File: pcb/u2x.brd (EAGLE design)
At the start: 100 x 100 mm, 9 parts, among them IC4 REG1117, SW20 324_SW, U1 UG-2864HSWEG01, U2 CY8C5868LTI-LP039, U3 USBC_16P

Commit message: started working on pcb
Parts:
- removed U1: UG-2864HSWEG01, lul:LUL_UG-2864HSWEG01_1.3_WRAPAROUND
- removed X2: (no value), bott:USB-A-H
- added JP1: (no value), adafruit_changed:2X20-BIG
- added X8: USB2, RPB:USB2
- X1: value (none) -> USB2; device bott:USB-A-H -> RPB:USB2
- moved X1 85.3 mm to (27.2, 3.05), turned to 90 degrees
- moved X3 62.3 mm to (8.89, 3.05), turned to 90 degrees
- moved SW20 23.6 mm to (5.08, 55.1)
- moved IC4 20.7 mm to (5.59, 63.8), turned to 90 degrees
- moved U2 14.0 mm to (31.0, 49.3)
- moved SD1 3.89 mm to (8.03, 18.9)
- moved U3 0.25 mm to (5.46, 47.0)
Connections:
- removed net VCC: U1.28
- removed net VLSS: U1.29
- net VDD: no longer U1.9
- net VSS: no longer U1.31, U1.32, U1.8
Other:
- board size 100 x 100 mm -> 56 x 85 mm
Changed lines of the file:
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@@
 <board>
 <plain>
-<wire x1="0" y1="100" x2="0" y2="0" width="0" layer="20"/>
-<wire x1="0" y1="0" x2="100" y2="0" width="0" layer="20"/>
-<wire x1="100" y1="0" x2="100" y2="100" width="0" layer="20"/>
-<wire x1="100" y1="100" x2="0" y2="100" width="0" layer="20"/>
-<rectangle x1="22.4834" y1="56.8782" x2="56.4834" y2="79.8782" layer="51"/>
-<rectangle x1="19.372" y1="28.992" x2="59.372" y2="43.992" layer="51" rot="R90"/>
-<rectangle x1="62.23" y1="40.894" x2="81.83" y2="65.894" layer="51"/>
+<wire x1="0" y1="85" x2="0" y2="0" width="0" layer="20"/>
+<wire x1="0" y1="0" x2="56" y2="0" width="0" layer="20"/>
+<wire x1="56" y1="0" x2="56" y2="85" width="0" layer="20"/>
+<wire x1="56" y1="85" x2="0" y2="85" width="0" layer="20"/>
 </plain>
 <attributes>
@@
 </autorouter>
 <elements>
-<element name="U3" library="my_usbc_16p" package="USBC_16P_FOOT" value="USBC_16P" x="5.461" y="47.2186" smashed="yes" rot="R270"/>
-<element name="U1" library="lul" package="LUL_UG-2864HSWEG01_1.3_WRAPAROUND" value="UG-2864HSWEG01" x="41.0784" y="7.5306" smashed="yes" rot="MR180"/>
-<element name="SD1" library="clock" package="TF-PULL" value="TF-HOLDER" x="8.7884" y="22.7076" smashed="yes" rot="R90">
-<attribute name="NAME" x="7.6884" y="30.4076" size="1.016" layer="25" ratio="18"/>
-</element>
-<element name="IC4" library="clock" package="SOT223" value="REG1117" x="19.05" y="48.006" smashed="yes" rot="R270">
-<attribute name="MF" value="" x="31.75" y="55.626" size="1.778" layer="27" rot="R270" display="off"/>
-<attribute name="MPN" value="REG1117" x="31.75" y="55.626" size="1.778" layer="27" rot="R270" display="off"/>
-<attribute name="NAME" x="23.368" y="50.546" size="1.27" layer="25" ratio="10" rot="R270"/>
-<attribute name="OC_FARNELL" value="1097566" x="31.75" y="55.626" size="1.778" layer="27" rot="R270" display="off"/>
-<attribute name="OC_NEWARK" value="14P6981" x="31.75" y="55.626" size="1.778" layer="27" rot="R270" display="off"/>
-<attribute name="VALUE" x="13.208" y="50.8" size="1.27" layer="27" ratio="10" rot="R270"/>
-</element>
-<element name="SW20" library="3pos_slide_switch_centered" package="342_SWICH_FOOT" value="324_SW" x="20.066" y="36.83" smashed="yes"/>
-<element name="X1" library="bott" package="USB-A-H" value="" x="36.322" y="87.884" smashed="yes" rot="R270">
-<attribute name="NAME" x="40.132" y="82.169" size="1.27" layer="25"/>
-</element>
-<element name="X2" library="bott" package="USB-A-H" value="" x="12.192" y="84.582" smashed="yes">
-<attribute name="NAME" x="17.907" y="88.392" size="1.27" layer="25" rot="R90"/>
-</element>
-<element name="X3" library="bott" package="USB-A-H" value="" x="12.192" y="65.278" smashed="yes">
-<attribute name="NAME" x="17.907" y="69.088" size="1.27" layer="25" rot="R90"/>
-</element>
-<element name="U2" library="SparkFun-IC-Microcontroller" package="QFN-68" value="CY8C5868LTI-LP039" x="39.37" y="38.1" smashed="yes">
-<attribute name="NAME" x="39.37" y="42.545" size="0.6096" layer="25" font="vector" ratio="20" align="bottom-center"/>
-<attribute name="PROD_ID" value="IC-12391" x="39.37" y="38.1" size="1.778" layer="27" display="off"/>
-<attribute name="VALUE" x="39.37" y="33.02" size="0.6096" layer="27" font="vector" ratio="20" align="bottom-center"/>
+<element name="U3" library="my_usbc_16p" package="USBC_16P_FOOT" value="USBC_16P" x="5.461" y="46.9646" smashed="yes" rot="R270"/>
+<element name="SD1" library="clock" package="TF-PULL" value="TF-HOLDER" x="8.0264" y="18.8976" smashed="yes" rot="R90">
+<attribute name="NAME" x="6.9264" y="26.5976" size="1.016" layer="25" ratio="18"/>
+</element>
+<element name="IC4" library="clock" package="SOT223" value="REG1117" x="5.588" y="63.754" smashed="yes" rot="R90">
+<attribute name="MF" value="" x="-7.112" y="56.134" size="1.778" layer="27" rot="R90" display="off"/>
+<attribute name="MPN" value="REG1117" x="-7.112" y="56.134" size="1.778" layer="27" rot="R90" display="off"/>
+<attribute name="NAME" x="1.27" y="61.214" size="1.27" layer="25" ratio="10" rot="R90"/>
+<attribute name="OC_FARNELL" value="1097566" x="-7.112" y="56.134" size="1.778" layer="27" rot="R90" display="off"/>
+<attribute name="OC_NEWARK" value="14P6981" x="-7.112" y="56.134" size="1.778" layer="27" rot="R90" display="off"/>
+<attribute name="VALUE" x="11.43" y="60.96" size="1.27" layer="27" ratio="10" rot="R90"/>
+</element>
+<element name="SW20" library="3pos_slide_switch_centered" package="342_SWICH_FOOT" value="324_SW" x="5.08" y="55.118" smashed="yes"/>
+<element name="X3" library="bott" package="USB-A-H" value="" x="8.89" y="3.048" smashed="yes" rot="R90">
+<attribute name="NAME" x="5.08" y="8.763" size="1.27" layer="25" rot="R180"/>
+</element>
+<element name="U2" library="SparkFun-IC-Microcontroller" package="QFN-68" value="CY8C5868LTI-LP039" x="30.988" y="49.276" smashed="yes">
+<attribute name="NAME" x="30.988" y="53.721" size="0.6096" layer="25" font="vector" ratio="20" align="bottom-center"/>
+<attribute name="PROD_ID" value="IC-12391" x="30.988" y="49.276" size="1.778" layer="27" display="off"/>
+<attribute name="VALUE" x="30.988" y="44.196" size="0.6096" layer="27" font="vector" ratio="20" align="bottom-center"/>
+</element>
+<element name="JP1" library="adafruit_changed" package="2X20-BIG" value="" x="50.292" y="51.816" smashed="yes" rot="R90">
+<attribute name="NAME" x="47.117" y="26.416" size="1.27" layer="25" ratio="10" rot="R90"/>
+<attribute name="VALUE" x="54.737" y="26.416" size="1.27" layer="27" rot="R90"/>
+</element>
+<element name="X8" library="RPB" package="USB2" value="USB2" x="45.72" y="3.048" smashed="yes" rot="R90">
+<attribute name="MF" value="" x="45.72" y="3.048" size="1.778" layer="27" rot="R90" display="off"/>
+<attribute name="MPN" value="" x="45.72" y="3.048" size="1.778" layer="27" rot="R90" display="off"/>
+<attribute name="NAME" x="38.72" y="-4.952" size="1.27" layer="25" rot="R90"/>
+<attribute name="OC_FARNELL" value="unknown" x="45.72" y="3.048" size="1.778" layer="27" rot="R90" display="off"/>
+<attribute name="OC_NEWARK" value="unknown" x="45.72" y="3.048" size="1.778" layer="27" rot="R90" display="off"/>
+<attribute name="VALUE" x="51.22" y="0.048" size="1.27" layer="27" rot="R180"/>
+</element>
+<element name="X1" library="RPB" package="USB2" value="USB2" x="27.178" y="3.048" smashed="yes" rot="R90">
+<attribute name="MF" value="" x="27.178" y="3.048" size="1.778" layer="27" rot="R90" display="off"/>
+<attribute name="MPN" value="" x="27.178" y="3.048" size="1.778" layer="27" rot="R90" display="off"/>
+<attribute name="NAME" x="20.178" y="-4.952" size="1.27" layer="25" rot="R90"/>
+<attribute name="OC_FARNELL" value="unknown" x="27.178" y="3.048" size="1.778" layer="27" rot="R90" display="off"/>
+<attribute name="OC_NEWARK" value="unknown" x="27.178" y="3.048" size="1.778" layer="27" rot="R90" display="off"/>
+<attribute name="VALUE" x="32.678" y="0.048" size="1.27" layer="27" rot="R180"/>
 </element>
 </elements>
@@
 <signal name="GND">
 <polygon width="0.1524" layer="1" isolate="0.254">
-<vertex x="0" y="100"/>
+<vertex x="0" y="85"/>
 <vertex x="0" y="0"/>
-<vertex x="100" y="0"/>
-<vertex x="100" y="100"/>
+<vertex x="56" y="0"/>
+<vertex x="56" y="85"/>
 </polygon>
 <contactref element="IC4" pad="1"/>
@@
 <signal name="+3V3">
 <polygon width="0.1524" layer="16" isolate="0.254">
-<vertex x="0" y="100"/>
-<vertex x="100" y="100"/>
-<vertex x="100" y="0"/>
+<vertex x="0" y="85"/>
+<vertex x="56" y="85"/>
+<vertex x="56" y="0"/>
 <vertex x="0" y="0"/>
 </polygon>
 </signal>
-<signal name="VCC">
-<contactref element="U1" pad="28"/>
-</signal>
 <signal name="VDD">
-<contactref element="U1" pad="9"/>
 <contactref element="SD1" pad="4"/>
-<wire x1="16.4084" y1="23.8076" x2="37.8284" y2="7.5306" width="0" layer="19" extent="1-1"/>
-</signal>
-<signal name="VLSS">
-<contactref element="U1" pad="29"/>
 </signal>
 <signal name="VSS">
-<contactref element="U1" pad="8"/>
-<contactref element="U1" pad="31"/>
-<contactref element="U1" pad="32"/>
 <contactref element="SD1" pad="6"/>
-<wire x1="37.3284" y1="7.5306" x2="50.4784" y2="9.7706" width="0" layer="19" extent="1-1"/>
-<wire x1="31.6284" y1="9.7706" x2="37.3284" y2="7.5306" width="0" layer="19" extent="1-1"/>
-<wire x1="16.4084" y1="26.0076" x2="31.6284" y2="9.7706" width="0" layer="19" extent="1-1"/>
 </signal>
 </signals>

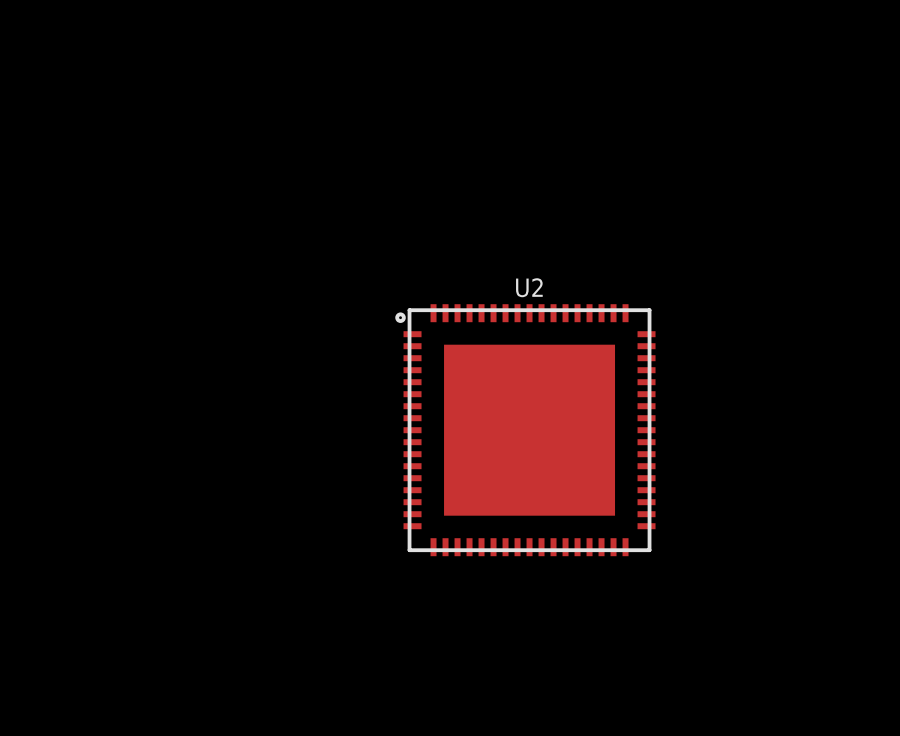
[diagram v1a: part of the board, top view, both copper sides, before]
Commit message: f1c100s library done
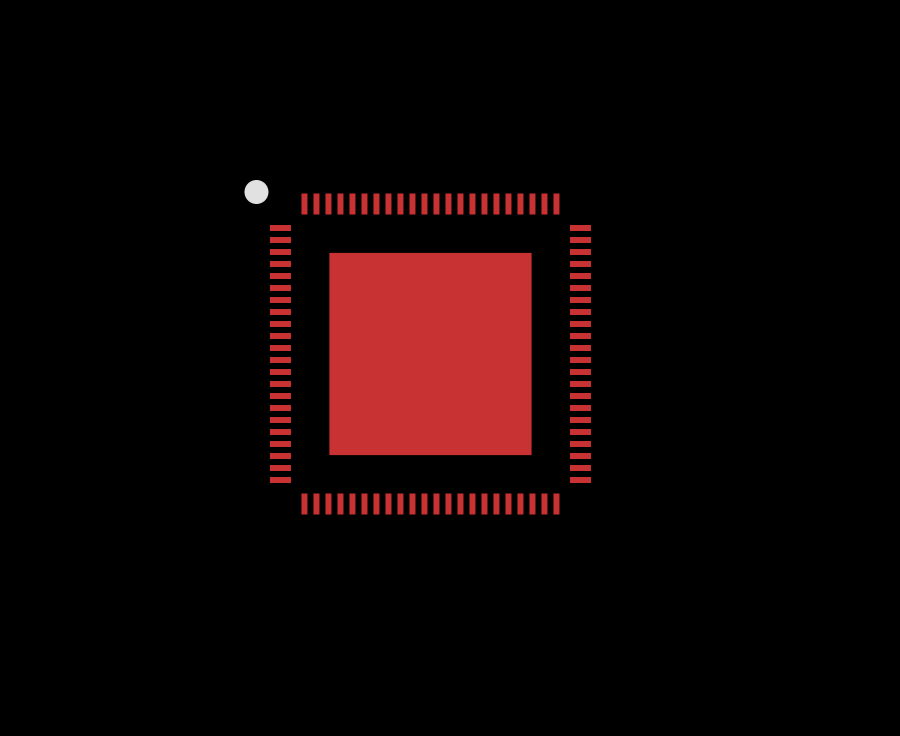
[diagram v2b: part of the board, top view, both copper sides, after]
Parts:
- removed U2: CY8C5868LTI-LP039, SparkFun-IC-Microcontroller:QFN-68
- added U$1: F1C100S_DEV, f1c100s:MQFN88
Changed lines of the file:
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@@
 <attribute name="NAME" x="5.08" y="8.763" size="1.27" layer="25" rot="R180"/>
-</element>
-<element name="U2" library="SparkFun-IC-Microcontroller" package="QFN-68" value="CY8C5868LTI-LP039" x="30.988" y="49.276" smashed="yes">
-<attribute name="NAME" x="30.988" y="53.721" size="0.6096" layer="25" font="vector" ratio="20" align="bottom-center"/>
-<attribute name="PROD_ID" value="IC-12391" x="30.988" y="49.276" size="1.778" layer="27" display="off"/>
-<attribute name="VALUE" x="30.988" y="44.196" size="0.6096" layer="27" font="vector" ratio="20" align="bottom-center"/>
 </element>
 <element name="JP1" library="adafruit_changed" package="2X20-BIG" value="" x="50.292" y="51.816" smashed="yes" rot="R90">
@@
 <attribute name="VALUE" x="32.678" y="0.048" size="1.27" layer="27" rot="R180"/>
 </element>
+<element name="U$1" library="f1c100s" package="MQFN88" value="F1C100S_DEV" x="27.686" y="51.816" smashed="yes"/>
 </elements>
 <signals>

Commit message: added more resources, worked on PCB, new libraries, placement, USB chip selection, OLED libarary
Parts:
- removed IC4: REG1117, clock:SOT223
- added IC1: LD117AS33TR, v-reg:SOT223
- added IC2: LD117AS25TR, v-reg:SOT223
- added IC3: LD117AS12TR, v-reg:SOT223
- added U$2, U$3, U$4, U$5: M2.5HOLE, f1c100s:M2.5HOLE
- added U1: USB251XB, USB251xB:QFN-36
- added U2: (no value), lul:LUL_UG-2864HSWEG01_1.3_WRAPAROUND
- moved SD1 61.2 mm to (27.8, 76.8), turned to 0 degrees
- moved X3 37.1 mm to (46.0, 3.05)
- moved U3 26.9 mm to (4.00, 73.8)
- moved SW20 19.3 mm to (5.59, 35.8), turned to 180 degrees
- moved X8 18.7 mm to (27.0, 3.00)
- moved X1 18.2 mm to (9.00, 3.00)
- moved U$1 5.34 mm to (22.4, 52.1)
- moved JP1 2.31 mm to (52.5, 52.5)
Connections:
- removed net GND: IC4.1
- new net VCC: U2.15
- net VDD: now also U2.7
- net VSS: now also U2.16, U2.17, U2.6

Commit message: added ch340, working on power
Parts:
- added C1, C2, C29, C3: 10uF, clock:0805@1
- added C27: 47uF, clock:C1210
- added LED1, LED3: (no value), adafruit:CHIP-LED0805
- added R1, R9: 5.1K, joyAnalog:0805
- added R3, R4: 1K, SparkFun-Passives:0805
- added U5: CH340C, SparkFun-IC-Comms:SO016
- moved SD1 10.8 mm to (38.6, 76.4)
- moved SW20 7.18 mm to (6.60, 28.7)
- moved IC3 3.29 mm to (4.83, 42.7)
- moved IC2 2.59 mm to (4.83, 52.6)
- moved IC1 1.24 mm to (4.83, 62.6)
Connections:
- new net +3V3: C27.1, IC1.4, IC3.3
- new net +5V: C1.2, C29.2, IC1.3, IC2.3, U3.A4B9, U3.B4A9
- new net GND: C1.1, C2.1, C27.2, C29.1, C3.1, IC1.1, IC2.1, IC3.1, R1.2, R9.2, U3.A1B12, U3.B11A12, U3.P$13, U3.P$14, U3.P$15, U3.P$16
- new net N$1: R9.1, U3.A5
- new net N$2: R1.1, U3.B5
- new net N$3: C2.2, IC2.4
- new net N$4: C3.2, IC3.4
- new net N$5: LED1.C, R4.2
- new net N$6: LED3.C, R3.2

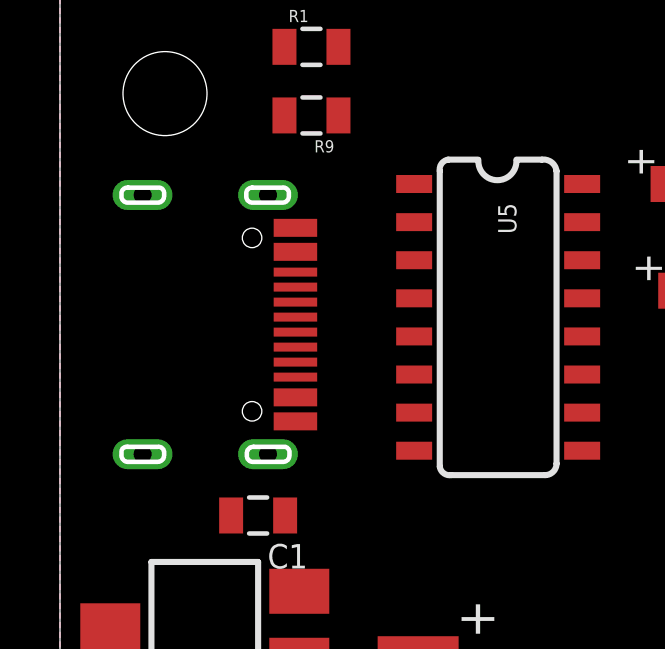
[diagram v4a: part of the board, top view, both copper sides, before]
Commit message: switched to sparkfuns usbc
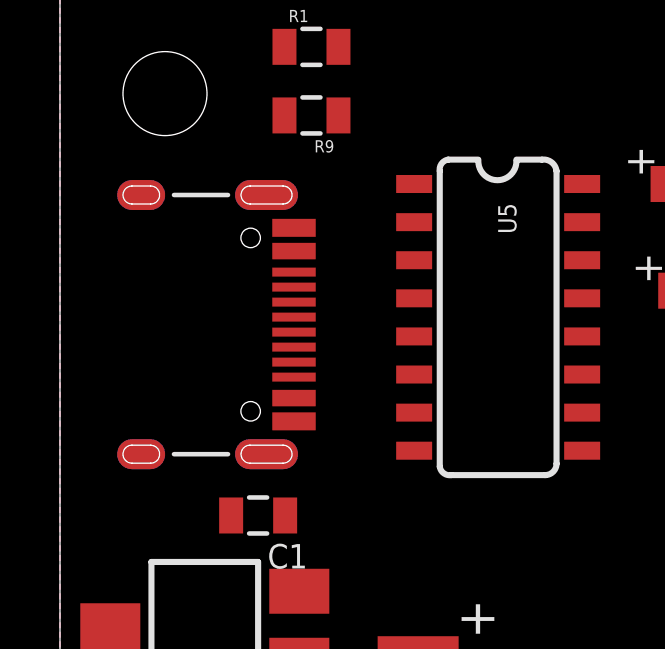
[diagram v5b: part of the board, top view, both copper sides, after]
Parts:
- removed U3: USBC_16P, my_usbc_16p:USBC_16P_FOOT
- added J2: (no value), SparkFun-Connectors:USB-C-16P
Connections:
- removed net N$1: R9.1, U3.A5
- new net N$7: J2.B5, R1.1
- net +5V: now also J2.VBUS1, J2.VBUS2; no longer U3.A4B9, U3.B4A9
- net GND: now also J2.GND, J2.GND2, J2.SHLD1, J2.SHLD2, J2.SHLD3, J2.SHLD4, J2.SHLD5, J2.SHLD6, J2.SHLD7, J2.SHLD8; no longer U3.A1B12, U3.B11A12, U3.P$13, U3.P$14, U3.P$15, U3.P$16
- net N$2: now also J2.A5, R9.1; no longer R1.1, U3.B5
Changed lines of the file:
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@@
 <setting verticaltext="up"/>
 </settings>
-<grid distance="5" unitdist="mil" unit="mil" style="lines" multiple="1" display="no" altdistance="1" altunitdist="mil" altunit="mil"/>
+<grid distance="5" unitdist="mil" unit="mm" style="lines" multiple="1" display="no" altdistance="1" altunitdist="mil" altunit="mil"/>
 <layers>
 <layer number="1" name="Top" color="4" fill="1" visible="yes" active="yes"/>
@@
 </autorouter>
 <elements>
-<element name="U3" library="my_usbc_16p" package="USBC_16P_FOOT" value="USBC_16P" x="4" y="73.8" smashed="yes" rot="R270"/>
 <element name="SD1" library="clock" package="TF-PULL" value="TF-HOLDER" x="38.5826" y="76.4286" smashed="yes">
 <attribute name="NAME" x="46.2826" y="77.5286" size="1.016" layer="25" ratio="18" rot="R270"/>
@@
 <element name="R3" library="SparkFun-Passives" package="0805" value="1K" x="25.527" y="78.867" smashed="yes" rot="R180">
 <attribute name="NAME" x="26.289" y="78.0415" size="0.8128" layer="25" rot="R180"/>
+</element>
+<element name="J2" library="SparkFun-Connectors" package="USB-C-16P" value="" x="7.8" y="73.8" smashed="yes" rot="R270">
+<attribute name="PROD_ID" value="CONN-14122" x="7.927" y="73.8" size="1.778" layer="27" rot="R270" display="off"/>
+<attribute name="VALUE" x="3.99" y="73.8" size="0.762" layer="27" rot="R270" align="center"/>
 </element>
 </elements>
@@
 <contactref element="R9" pad="2"/>
 <contactref element="R1" pad="2"/>
-<contactref element="U3" pad="P$15"/>
-<contactref element="U3" pad="P$16"/>
-<contactref element="U3" pad="P$13"/>
-<contactref element="U3" pad="P$14"/>
-<contactref element="U3" pad="B11A12"/>
-<contactref element="U3" pad="A1B12"/>
 <contactref element="IC1" pad="1"/>
 <contactref element="C27" pad="2"/>
@@
 <contactref element="C2" pad="1"/>
 <contactref element="C3" pad="1"/>
+<contactref element="J2" pad="SHLD1" route="any" routetag="J1.SHLD"/>
+<contactref element="J2" pad="SHLD8" route="any" routetag="J1.SHLD"/>
+<contactref element="J2" pad="SHLD6" route="any" routetag="J1.SHLD"/>
+<contactref element="J2" pad="SHLD3" route="any" routetag="J1.SHLD"/>
+<contactref element="J2" pad="SHLD4" route="any" routetag="J1.SHLD"/>
+<contactref element="J2" pad="SHLD7" route="any" routetag="J1.SHLD"/>
+<contactref element="J2" pad="SHLD5" route="any" routetag="J1.SHLD"/>
+<contactref element="J2" pad="SHLD2" route="any" routetag="J1.SHLD"/>
+<contactref element="J2" pad="GND2"/>
+<contactref element="J2" pad="GND"/>
 </signal>
 <signal name="+3V3">
@@
 <contactref element="U2" pad="15"/>
 </signal>
-<signal name="N$1">
-<contactref element="U3" pad="A5"/>
-<contactref element="R9" pad="1"/>
-<wire x1="7.8475" y1="75.05" x2="9.282" y2="80.772" width="0" layer="19" extent="1-1"/>
-</signal>
-<signal name="N$2">
-<contactref element="U3" pad="B5"/>
-<contactref element="R1" pad="1"/>
-<wire x1="7.8475" y1="72.05" x2="7.482" y2="83.058" width="0" layer="19" extent="1-1"/>
-</signal>
 <signal name="+5V">
-<contactref element="U3" pad="A4B9"/>
-<contactref element="U3" pad="B4A9"/>
 <contactref element="IC1" pad="3"/>
 <contactref element="IC2" pad="3"/>
 <contactref element="C29" pad="2"/>
 <contactref element="C1" pad="2"/>
-<wire x1="7.8475" y1="71.375" x2="7.8475" y2="76.225" width="0" layer="19" extent="1-1"/>
-<wire x1="5.704" y1="67.437" x2="7.8475" y2="71.375" width="0" layer="19" extent="1-1"/>
+<contactref element="J2" pad="VBUS2"/>
+<contactref element="J2" pad="VBUS1"/>
+<wire x1="7.8" y1="71.35" x2="7.8" y2="76.25" width="0" layer="19" extent="1-1"/>
+<wire x1="5.704" y1="67.437" x2="7.8" y2="71.35" width="0" layer="19" extent="1-1"/>
 <wire x1="7.976" y1="64.911" x2="5.704" y2="67.437" width="0" layer="19" extent="1-1"/>
 <wire x1="6.212" y1="57.785" x2="7.976" y2="64.911" width="0" layer="19" extent="1-1"/>
@@
 <contactref element="LED1" pad="C"/>
 <contactref element="R4" pad="2"/>
-<wire x1="24.627" y1="75.438" x2="22.64" y2="74.93" width="0" layer="19" extent="1-1"/>
+<wire x1="22.64" y1="74.93" x2="24.627" y2="75.438" width="0" layer="19" extent="1-1"/>
 </signal>
 <signal name="N$6">
 <contactref element="LED3" pad="C"/>
 <contactref element="R3" pad="2"/>
-<wire x1="24.627" y1="78.867" x2="22.386" y2="78.486" width="0" layer="19" extent="1-1"/>
+<wire x1="22.386" y1="78.486" x2="24.627" y2="78.867" width="0" layer="19" extent="1-1"/>
+</signal>
+<signal name="N$2">
+<contactref element="J2" pad="A5"/>
+<contactref element="R9" pad="1"/>
+<wire x1="7.8" y1="75.05" x2="9.282" y2="80.772" width="0" layer="19" extent="1-1"/>
+</signal>
+<signal name="N$7">
+<contactref element="J2" pad="B5"/>
+<contactref element="R1" pad="1"/>
+<wire x1="7.8" y1="72.05" x2="7.482" y2="83.058" width="0" layer="19" extent="1-1"/>
 </signal>
 </signals>
